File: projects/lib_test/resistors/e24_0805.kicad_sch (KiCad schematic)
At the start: 171 parts

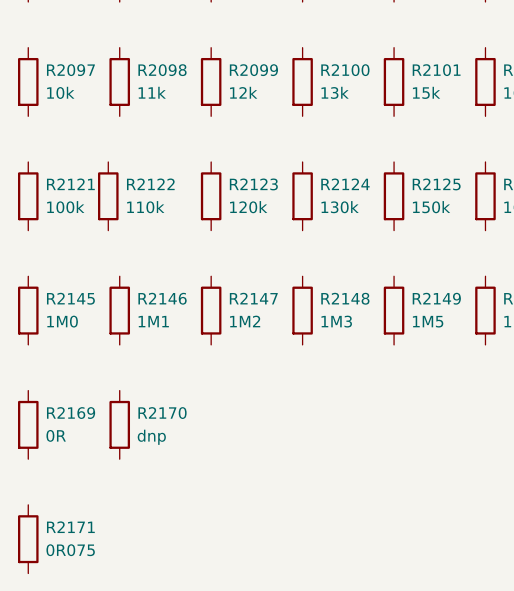
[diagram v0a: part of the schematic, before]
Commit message: add test project for resistors
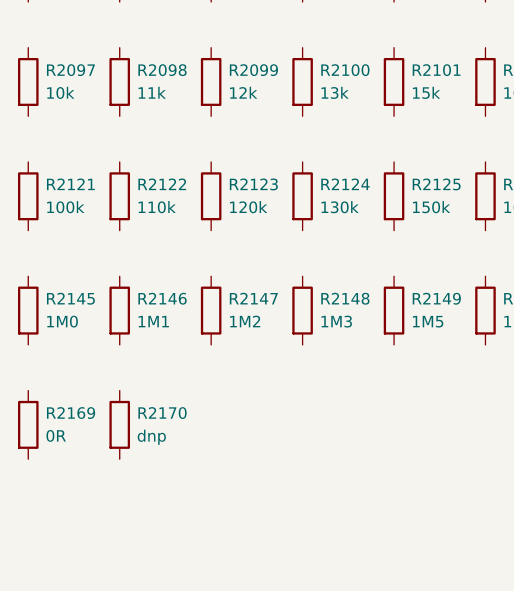
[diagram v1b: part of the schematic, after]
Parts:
- removed R2171: 0R075, lily_footprints:res_2512, symbol lily_symbols:res_0R075_1%_3W_2512
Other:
- company: LilyTronics -> (none)
- title: Lily KiCad Library test -> (none)

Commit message: updated test projects
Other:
- title: (none) -> Resistors
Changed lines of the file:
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@@
 (kicad_sch
-	(version 20231120)
+	(version 20250114)
 	(generator "eeschema")
-	(generator_version "8.0")
+	(generator_version "9.0")
 	(paper "A4")
+	(title_block
+		(title "Resistors")
+		(date "2025-05-24")
+		(rev "1")
+		(comment 1 "-")
+		(comment 2 "-")
+	)
 	(symbol
 		(lib_id "lily_symbols:res_3R3_1%_125mW_0805")

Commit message: updated resistors test design
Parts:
- R2001: JLCPCB_ID C25271 -> C131397; JLCPCB_STATUS Basic -> (none); Lily_ID 1913-11000 -> NO_ID; Manufacturer Uniroyal Electronics -> YAGEO; Manufacturer_ID 0805W8F100KT5E -> RC0805FR-071RL
- R2002: JLCPCB_ID C17376 -> C137574; JLCPCB_STATUS Extended -> (none); Lily_ID 1913-11100 -> NO_ID; Manufacturer Uniroyal Electronics -> YAGEO; Manufacturer_ID 0805W8F110KT5E -> RC0805FR-071R1L
- R2003: JLCPCB_ID C17381 -> C137573; JLCPCB_STATUS Extended -> (none); Lily_ID 1913-11200 -> NO_ID; Manufacturer Uniroyal Electronics -> YAGEO; Manufacturer_ID 0805W8F120KT5E -> RC0805FR-071R2L
- R2004: JLCPCB_ID C17385 -> C185293; JLCPCB_STATUS Extended -> (none); Lily_ID 1913-11300 -> NO_ID; Manufacturer Uniroyal Electronics -> YAGEO; Manufacturer_ID 0805W8F130KT5E -> RC0805FR-071R3L
- R2005: JLCPCB_ID C17392 -> C137572; JLCPCB_STATUS Extended -> (none); Lily_ID 1913-11500 -> NO_ID; Manufacturer Uniroyal Electronics -> YAGEO; Manufacturer_ID 0805W8F150KT5E -> RC0805FR-071R5L
- R2006: JLCPCB_ID C25272 -> C137571; JLCPCB_STATUS Extended -> (none); Lily_ID 1913-11600 -> NO_ID; Manufacturer Uniroyal Electronics -> YAGEO; Manufacturer_ID 0805W8F160KT5E -> RC0805FR-071R6L
- R2007: JLCPCB_ID C17400 -> C327106; JLCPCB_STATUS Extended -> (none); Lily_ID 1913-11800 -> NO_ID; Manufacturer Uniroyal Electronics -> YAGEO; Manufacturer_ID 0805W8F180KT5E -> RC0805FR-071R8L
- R2008: JLCPCB_ID C17606 -> C114246; JLCPCB_STATUS Extended preferred -> (none); Lily_ID 1913-12000 -> NO_ID; Manufacturer Uniroyal Electronics -> YAGEO; Manufacturer_ID 0805W8F200KT5E -> RC0805FR-072RL
- R2009: JLCPCB_ID C17521 -> C137549; JLCPCB_STATUS Basic -> (none); Lily_ID 1913-12200 -> NO_ID; Manufacturer Uniroyal Electronics -> YAGEO; Manufacturer_ID 0805W8F220KT5E -> RC0805FR-072R2L
- R2010: JLCPCB_ID C17528 -> C137548; JLCPCB_STATUS Extended -> (none); Lily_ID 1913-12400 -> NO_ID; Manufacturer Uniroyal Electronics -> YAGEO; Manufacturer_ID 0805W8F240KT5E -> RC0805FR-072R4L
- R2011: JLCPCB_ID C17532 -> C137547; JLCPCB_STATUS Extended -> (none); Lily_ID 1913-12700 -> NO_ID; Manufacturer Uniroyal Electronics -> YAGEO; Manufacturer_ID 0805W8F270KT5E -> RC0805FR-072R7L
- R2012: JLCPCB_ID C17660 -> C137528; JLCPCB_STATUS Extended -> (none); Lily_ID 1913-13000 -> NO_ID; Manufacturer Uniroyal Electronics -> YAGEO; Manufacturer_ID 0805W8F300KT5E -> RC0805FR-073RL
- R2013: JLCPCB_ID C16257 -> C137531; JLCPCB_STATUS Extended -> (none); Lily_ID 1913-13300 -> NO_ID; Manufacturer Uniroyal Electronics -> YAGEO; Manufacturer_ID 0805W8F330KT5E -> RC0805FR-073R3L
- R2014: JLCPCB_ID C17610 -> C137530; JLCPCB_STATUS Extended -> (none); Lily_ID 1913-13600 -> NO_ID; Manufacturer Uniroyal Electronics -> YAGEO; Manufacturer_ID 0805W8F360KT5E -> RC0805FR-073R6L
- R2015: JLCPCB_ID C17615 -> C137529; JLCPCB_STATUS Extended -> (none); Lily_ID 1913-13900 -> NO_ID; Manufacturer Uniroyal Electronics -> YAGEO; Manufacturer_ID 0805W8F390KT5E -> RC0805FR-073R9L
- R2016: JLCPCB_ID C17669 -> C137514; JLCPCB_STATUS Extended -> (none); Lily_ID 1913-14300 -> NO_ID; Manufacturer Uniroyal Electronics -> YAGEO; Manufacturer_ID 0805W8F430KT5E -> RC0805FR-074R3L
- R2017: JLCPCB_ID C17675 -> C137513; JLCPCB_STATUS Basic -> (none); Lily_ID 1913-14700 -> NO_ID; Manufacturer Uniroyal Electronics -> YAGEO; Manufacturer_ID 0805W8F470KT5E -> RC0805FR-074R7L
- R2018: JLCPCB_ID C17724 -> C114539; JLCPCB_STATUS Basic -> (none); Lily_ID 1913-15100 -> NO_ID; Manufacturer Uniroyal Electronics -> YAGEO; Manufacturer_ID 0805W8F510KT5E -> RC0805FR-075R1L
- R2019: JLCPCB_ID C17729 -> C275644; JLCPCB_STATUS Extended -> (none); Lily_ID 1913-15600 -> NO_ID; Manufacturer Uniroyal Electronics -> YAGEO; Manufacturer_ID 0805W8F560KT5E -> RC0805FR-075R6L
- R2020: JLCPCB_ID C17768 -> C483193; JLCPCB_STATUS Extended -> (none); Lily_ID 1913-16200 -> NO_ID; Manufacturer Uniroyal Electronics -> YAGEO; Manufacturer_ID 0805W8F620KT5E -> RC0805FR-076R2L
- R2021: JLCPCB_ID C17774 -> C137492; JLCPCB_STATUS Extended -> (none); Lily_ID 1913-16800 -> NO_ID; Manufacturer Uniroyal Electronics -> YAGEO; Manufacturer_ID 0805W8F680KT5E -> RC0805FR-076R8L
- R2022: JLCPCB_ID C17809 -> C483222; JLCPCB_STATUS Extended -> (none); Lily_ID 1913-17500 -> NO_ID; Manufacturer Uniroyal Electronics -> YAGEO; Manufacturer_ID 0805W8F750KT5E -> RC0805FR-077R5L
- R2023: JLCPCB_ID C17830 -> C185282; JLCPCB_STATUS Extended -> (none); Lily_ID 1913-18200 -> NO_ID; Manufacturer Uniroyal Electronics -> YAGEO; Manufacturer_ID 0805W8F820KT5E -> RC0805FR-078R2L
- R2024: JLCPCB_ID C17857 -> C483254; JLCPCB_STATUS Extended -> (none); Lily_ID 1913-19100 -> NO_ID; Manufacturer Uniroyal Electronics -> YAGEO; Manufacturer_ID 0805W8F910KT5E -> RC0805FR-079R1L
- R2025: JLCPCB_ID C17415 -> C96347; JLCPCB_STATUS Basic -> (none); Lily_ID 1913-11001 -> NO_ID; Manufacturer Uniroyal Electronics -> YAGEO; Manufacturer_ID 0805W8F100JT5E -> RC0805FR-0710RL
- R2026: JLCPCB_ID C17430 -> C185296; JLCPCB_STATUS Extended -> (none); Lily_ID 1913-11101 -> NO_ID; Manufacturer Uniroyal Electronics -> YAGEO; Manufacturer_ID 0805W8F110JT5E -> RC0805FR-0711RL
- R2027: JLCPCB_ID C17445 -> C137594; JLCPCB_STATUS Extended -> (none); Lily_ID 1913-11201 -> NO_ID; Manufacturer Uniroyal Electronics -> YAGEO; Manufacturer_ID 0805W8F120JT5E -> RC0805FR-0712RL
- R2028: JLCPCB_ID C25268 -> C273810; JLCPCB_STATUS Extended -> (none); Lily_ID 1913-11301 -> NO_ID; Manufacturer Uniroyal Electronics -> YAGEO; Manufacturer_ID 0805W8F130JT5E -> RC0805FR-0713RL
- R2029: JLCPCB_ID C17480 -> C137590; JLCPCB_STATUS Extended preferred -> (none); Lily_ID 1913-11501 -> NO_ID; Manufacturer Uniroyal Electronics -> YAGEO; Manufacturer_ID 0805W8F150JT5E -> RC0805FR-0715RL
- R2030: JLCPCB_ID C17491 -> C137587; JLCPCB_STATUS Extended -> (none); Lily_ID 1913-11601 -> NO_ID; Manufacturer Uniroyal Electronics -> YAGEO; Manufacturer_ID 0805W8F160JT5E -> RC0805FR-0716RL
- R2031: JLCPCB_ID C17507 -> C137583; JLCPCB_STATUS Extended -> (none); Lily_ID 1913-11801 -> NO_ID; Manufacturer Uniroyal Electronics -> YAGEO; Manufacturer_ID 0805W8F180JT5E -> RC0805FR-0718RL
- R2032: JLCPCB_ID C17544 -> C114557; JLCPCB_STATUS Basic -> (none); Lily_ID 1913-12001 -> NO_ID; Manufacturer Uniroyal Electronics -> YAGEO; Manufacturer_ID 0805W8F200JT5E -> RC0805FR-0720RL
- R2033: JLCPCB_ID C17561 -> C107702; JLCPCB_STATUS Basic -> (none); Lily_ID 1913-12201 -> NO_ID; Manufacturer Uniroyal Electronics -> YAGEO; Manufacturer_ID 0805W8F220JT5E -> RC0805FR-0722RL
- R2034: JLCPCB_ID C17576 -> C185291; JLCPCB_STATUS Extended -> (none); Lily_ID 1913-12401 -> NO_ID; Manufacturer Uniroyal Electronics -> YAGEO; Manufacturer_ID 0805W8F240JT5E -> RC0805FR-0724RL
- R2035: JLCPCB_ID C17594 -> C163408; JLCPCB_STATUS Extended preferred -> (none); Lily_ID 1913-12701 -> NO_ID; Manufacturer Uniroyal Electronics -> YAGEO; Manufacturer_ID 0805W8F270JT5E -> RC0805FR-0727RL
- R2036: JLCPCB_ID C17622 -> C137545; JLCPCB_STATUS Extended -> (none); Lily_ID 1913-13001 -> NO_ID; Manufacturer Uniroyal Electronics -> YAGEO; Manufacturer_ID 0805W8F300JT5E -> RC0805FR-0730RL
- R2037: JLCPCB_ID C17634 -> C126353; JLCPCB_STATUS Basic -> (none); Lily_ID 1913-13301 -> NO_ID; Manufacturer Uniroyal Electronics -> YAGEO; Manufacturer_ID 0805W8F330JT5E -> RC0805FR-0733RL
- R2038: JLCPCB_ID C36524 -> C137536; JLCPCB_STATUS Extended -> (none); Lily_ID 1913-13601 -> NO_ID; Manufacturer Uniroyal Electronics -> YAGEO; Manufacturer_ID 0805W8F360JT5E -> RC0805FR-0736RL
- R2039: JLCPCB_ID C17659 -> C137534; JLCPCB_STATUS Extended -> (none); Lily_ID 1913-13901 -> NO_ID; Manufacturer Uniroyal Electronics -> YAGEO; Manufacturer_ID 0805W8F390JT5E -> RC0805FR-0739RL
- R2040: JLCPCB_ID C4368 -> C137523; JLCPCB_STATUS Extended -> (none); Lily_ID 1913-14301 -> NO_ID; Manufacturer Uniroyal Electronics -> YAGEO; Manufacturer_ID 0805W8F430JT5E -> RC0805FR-0743RL
- R2041: JLCPCB_ID C17714 -> C114541; JLCPCB_STATUS Basic -> (none); Lily_ID 1913-14701 -> NO_ID; Manufacturer Uniroyal Electronics -> YAGEO; Manufacturer_ID 0805W8F470JT5E -> RC0805FR-0747RL
- R2042: JLCPCB_ID C17738 -> C114537; JLCPCB_STATUS Basic -> (none); Lily_ID 1913-15101 -> NO_ID; Manufacturer Uniroyal Electronics -> YAGEO; Manufacturer_ID 0805W8F510JT5E -> RC0805FR-0751RL
- R2043: JLCPCB_ID C17757 -> C137507; JLCPCB_STATUS Extended preferred -> (none); Lily_ID 1913-15601 -> NO_ID; Manufacturer Uniroyal Electronics -> YAGEO; Manufacturer_ID 0805W8F560JT5E -> RC0805FR-0756RL
- R2044: JLCPCB_ID C17784 -> C185283; JLCPCB_STATUS Extended -> (none); Lily_ID 1913-16201 -> NO_ID; Manufacturer Uniroyal Electronics -> YAGEO; Manufacturer_ID 0805W8F620JT5E -> RC0805FR-0762RL
- R2045: JLCPCB_ID C17802 -> C137498; JLCPCB_STATUS Extended preferred -> (none); Lily_ID 1913-16801 -> NO_ID; Manufacturer Uniroyal Electronics -> YAGEO; Manufacturer_ID 0805W8F680JT5E -> RC0805FR-0768RL
- R2046: JLCPCB_ID C17820 -> C141697; JLCPCB_STATUS Extended -> (none); Lily_ID 1913-17501 -> NO_ID; Manufacturer Uniroyal Electronics -> YAGEO; Manufacturer_ID 0805W8F750JT5E -> RC0805FR-0775RL
- R2047: JLCPCB_ID C17841 -> C141699; JLCPCB_STATUS Extended -> (none); Lily_ID 1913-18201 -> NO_ID; Manufacturer Uniroyal Electronics -> YAGEO; Manufacturer_ID 0805W8F820JT5E -> RC0805FR-0782RL
- R2048: JLCPCB_ID C4407 -> C276315; JLCPCB_STATUS Extended -> (none); Lily_ID 1913-19101 -> NO_ID; Manufacturer Uniroyal Electronics -> YAGEO; Manufacturer_ID 0805W8F910JT5E -> RC0805FR-0791RL
- R2049: JLCPCB_ID C17408 -> C105577; JLCPCB_STATUS Basic -> (none); Lily_ID 1913-11002 -> NO_ID; Manufacturer Uniroyal Electronics -> YAGEO; Manufacturer_ID 0805W8F1000T5E -> RC0805FR-07100RL
- R2050: JLCPCB_ID C17423 -> C246031; JLCPCB_STATUS Extended -> (none); Lily_ID 1913-11102 -> NO_ID; Manufacturer Uniroyal Electronics -> YAGEO; Manufacturer_ID 0805W8F1100T5E -> RC0805FR-07110RL
- R2051: JLCPCB_ID C17437 -> C114245; JLCPCB_STATUS Basic -> (none); Lily_ID 1913-11202 -> NO_ID; Manufacturer Uniroyal Electronics -> YAGEO; Manufacturer_ID 0805W8F1200T5E -> RC0805FR-07120RL
- R2052: JLCPCB_ID C17451 -> C273821; JLCPCB_STATUS Extended -> (none); Lily_ID 1913-11302 -> NO_ID; Manufacturer Uniroyal Electronics -> YAGEO; Manufacturer_ID 0805W8F1300T5E -> RC0805FR-07130RL
- R2053: JLCPCB_ID C17471 -> C114523; JLCPCB_STATUS Basic -> (none); Lily_ID 1913-11502 -> NO_ID; Manufacturer Uniroyal Electronics -> YAGEO; Manufacturer_ID 0805W8F1500T5E -> RC0805FR-07150RL
- R2054: JLCPCB_ID C25269 -> C246032; JLCPCB_STATUS Extended -> (none); Lily_ID 1913-11602 -> NO_ID; Manufacturer Uniroyal Electronics -> YAGEO; Manufacturer_ID 0805W8F1600T5E -> RC0805FR-07160RL
- R2055: JLCPCB_ID C25270 -> C137585; JLCPCB_STATUS Extended preferred -> (none); Lily_ID 1913-11802 -> NO_ID; Manufacturer Uniroyal Electronics -> YAGEO; Manufacturer_ID 0805W8F1800T5E -> RC0805FR-07180RL
- R2056: JLCPCB_ID C17540 -> C114567; JLCPCB_STATUS Basic -> (none); Lily_ID 1913-12002 -> NO_ID; Manufacturer Uniroyal Electronics -> YAGEO; Manufacturer_ID 0805W8F2000T5E -> RC0805FR-07200RL
- R2057: JLCPCB_ID C17557 -> C114519; JLCPCB_STATUS Basic -> (none); Lily_ID 1913-12202 -> NO_ID; Manufacturer Uniroyal Electronics -> YAGEO; Manufacturer_ID 0805W8F2200T5E -> RC0805FR-07220RL
- R2058: JLCPCB_ID C17572 -> C185292; JLCPCB_STATUS Extended preferred -> (none); Lily_ID 1913-12402 -> NO_ID; Manufacturer Uniroyal Electronics -> YAGEO; Manufacturer_ID 0805W8F2400T5E -> RC0805FR-07240RL
- R2059: JLCPCB_ID C17590 -> C137558; JLCPCB_STATUS Extended preferred -> (none); Lily_ID 1913-12702 -> NO_ID; Manufacturer Uniroyal Electronics -> YAGEO; Manufacturer_ID 0805W8F2700T5E -> RC0805FR-07270RL
- R2060: JLCPCB_ID C17617 -> C114529; JLCPCB_STATUS Basic -> (none); Lily_ID 1913-13002 -> NO_ID; Manufacturer Uniroyal Electronics -> YAGEO; Manufacturer_ID 0805W8F3000T5E -> RC0805FR-07300RL
- R2061: JLCPCB_ID C17630 -> C105878; JLCPCB_STATUS Basic -> (none); Lily_ID 1913-13302 -> NO_ID; Manufacturer Uniroyal Electronics -> YAGEO; Manufacturer_ID 0805W8F3300T5E -> RC0805FR-07330RL
- R2062: JLCPCB_ID C17646 -> C137538; JLCPCB_STATUS Extended -> (none); Lily_ID 1913-13602 -> NO_ID; Manufacturer Uniroyal Electronics -> YAGEO; Manufacturer_ID 0805W8F3600T5E -> RC0805FR-07360RL
- R2063: JLCPCB_ID C17655 -> C114543; JLCPCB_STATUS Basic -> (none); Lily_ID 1913-13902 -> NO_ID; Manufacturer Uniroyal Electronics -> YAGEO; Manufacturer_ID 0805W8F3900T5E -> RC0805FR-07390RL
- R2064: JLCPCB_ID C42000 -> C137527; JLCPCB_STATUS Extended -> (none); Lily_ID 1913-14302 -> NO_ID; Manufacturer Uniroyal Electronics -> YAGEO; Manufacturer_ID 0805W8F4300T5E -> RC0805FR-07430RL
- R2065: JLCPCB_ID C17710 -> C114564; JLCPCB_STATUS Basic -> (none); Lily_ID 1913-14702 -> NO_ID; Manufacturer Uniroyal Electronics -> YAGEO; Manufacturer_ID 0805W8F4700T5E -> RC0805FR-07470RL
- R2066: JLCPCB_ID C17734 -> C114563; JLCPCB_STATUS Basic -> (none); Lily_ID 1913-15102 -> NO_ID; Manufacturer Uniroyal Electronics -> YAGEO; Manufacturer_ID 0805W8F5100T5E -> RC0805FR-07510RL
- R2067: JLCPCB_ID C28636 -> C114536; JLCPCB_STATUS Basic -> (none); Lily_ID 1913-15602 -> NO_ID; Manufacturer Uniroyal Electronics -> YAGEO; Manufacturer_ID 0805W8F5600T5E -> RC0805FR-07560RL
- R2068: JLCPCB_ID C17782 -> C137503; JLCPCB_STATUS Extended -> (none); Lily_ID 1913-16202 -> NO_ID; Manufacturer Uniroyal Electronics -> YAGEO; Manufacturer_ID 0805W8F6200T5E -> RC0805FR-07620RL
- R2069: JLCPCB_ID C17798 -> C114549; JLCPCB_STATUS Basic -> (none); Lily_ID 1913-16802 -> NO_ID; Manufacturer Uniroyal Electronics -> YAGEO; Manufacturer_ID 0805W8F6800T5E -> RC0805FR-07680RL
- R2070: JLCPCB_ID C17818 -> C114546; JLCPCB_STATUS Extended preferred -> (none); Lily_ID 1913-17502 -> NO_ID; Manufacturer Uniroyal Electronics -> YAGEO; Manufacturer_ID 0805W8F7500T5E -> RC0805FR-07750RL
- R2071: JLCPCB_ID C17837 -> C114544; JLCPCB_STATUS Extended preferred -> (none); Lily_ID 1913-18202 -> NO_ID; Manufacturer Uniroyal Electronics -> YAGEO; Manufacturer_ID 0805W8F8200T5E -> RC0805FR-07820RL
- R2072: JLCPCB_ID C17865 -> C141702; JLCPCB_STATUS Extended -> (none); Lily_ID 1913-19102 -> NO_ID; Manufacturer Uniroyal Electronics -> YAGEO; Manufacturer_ID 0805W8F9100T5E -> RC0805FR-07910RL
- R2073: JLCPCB_ID C17513 -> C95781; JLCPCB_STATUS Basic -> (none); Lily_ID 1913-11003 -> NO_ID; Manufacturer Uniroyal Electronics -> YAGEO; Manufacturer_ID 0805W8F1001T5E -> RC0805FR-071KL
- R2074: JLCPCB_ID C17375 -> C185294; JLCPCB_STATUS Extended -> (none); Lily_ID 1913-11103 -> NO_ID; Manufacturer Uniroyal Electronics -> YAGEO; Manufacturer_ID 0805W8F1101T5E -> RC0805FR-071K1L
- R2075: JLCPCB_ID C17379 -> C114526; JLCPCB_STATUS Basic -> (none); Lily_ID 1913-11203 -> NO_ID; Manufacturer Uniroyal Electronics -> YAGEO; Manufacturer_ID 0805W8F1201T5E -> RC0805FR-071K2L
- R2076: JLCPCB_ID C17384 -> C137582; JLCPCB_STATUS Extended -> (none); Lily_ID 1913-11303 -> NO_ID; Manufacturer Uniroyal Electronics -> YAGEO; Manufacturer_ID 0805W8F1301T5E -> RC0805FR-071K3L
- R2077: JLCPCB_ID C4310 -> C114555; JLCPCB_STATUS Basic -> (none); Lily_ID 1913-11503 -> NO_ID; Manufacturer Uniroyal Electronics -> YAGEO; Manufacturer_ID 0805W8F1501T5E -> RC0805FR-071K5L
- R2078: JLCPCB_ID C17394 -> C137580; JLCPCB_STATUS Extended -> (none); Lily_ID 1913-11603 -> NO_ID; Manufacturer Uniroyal Electronics -> YAGEO; Manufacturer_ID 0805W8F1601T5E -> RC0805FR-071K6L
- R2079: JLCPCB_ID C17398 -> C137579; JLCPCB_STATUS Extended preferred -> (none); Lily_ID 1913-11803 -> NO_ID; Manufacturer Uniroyal Electronics -> YAGEO; Manufacturer_ID 0805W8F1801T5E -> RC0805FR-071K8L
- R2080: JLCPCB_ID C17604 -> C114572; JLCPCB_STATUS Basic -> (none); Lily_ID 1913-12003 -> NO_ID; Manufacturer Uniroyal Electronics -> YAGEO; Manufacturer_ID 0805W8F2001T5E -> RC0805FR-072KL
- R2081: JLCPCB_ID C17520 -> C114561; JLCPCB_STATUS Basic -> (none); Lily_ID 1913-12203 -> NO_ID; Manufacturer Uniroyal Electronics -> YAGEO; Manufacturer_ID 0805W8F2201T5E -> RC0805FR-072K2L
- R2082: JLCPCB_ID C17526 -> C114521; JLCPCB_STATUS Basic -> (none); Lily_ID 1913-12403 -> NO_ID; Manufacturer Uniroyal Electronics -> YAGEO; Manufacturer_ID 0805W8F2401T5E -> RC0805FR-072K4L
- R2083: JLCPCB_ID C17530 -> C114520; JLCPCB_STATUS Basic -> (none); Lily_ID 1913-12703 -> NO_ID; Manufacturer Uniroyal Electronics -> YAGEO; Manufacturer_ID 0805W8F2701T5E -> RC0805FR-072K7L
- R2084: JLCPCB_ID C17661 -> C126350; JLCPCB_STATUS Basic -> (none); Lily_ID 1913-13003 -> NO_ID; Manufacturer Uniroyal Electronics -> YAGEO; Manufacturer_ID 0805W8F3001T5E -> RC0805FR-073KL
- R2085: JLCPCB_ID C26010 -> C114531; JLCPCB_STATUS Basic -> (none); Lily_ID 1913-13303 -> NO_ID; Manufacturer Uniroyal Electronics -> YAGEO; Manufacturer_ID 0805W8F3301T5E -> RC0805FR-073K3L
- R2086: JLCPCB_ID C18359 -> C137533; JLCPCB_STATUS Extended preferred -> (none); Lily_ID 1913-13603 -> NO_ID; Manufacturer Uniroyal Electronics -> YAGEO; Manufacturer_ID 0805W8F3601T5E -> RC0805FR-073K6L
- R2087: JLCPCB_ID C17614 -> C114221; JLCPCB_STATUS Basic -> (none); Lily_ID 1913-13903 -> NO_ID; Manufacturer Uniroyal Electronics -> YAGEO; Manufacturer_ID 0805W8F3901T5E -> RC0805FR-073K9L
- R2088: JLCPCB_ID C17667 -> C137518; JLCPCB_STATUS Extended preferred -> (none); Lily_ID 1913-14303 -> NO_ID; Manufacturer Uniroyal Electronics -> YAGEO; Manufacturer_ID 0805W8F4301T5E -> RC0805FR-074K3L
- R2089: JLCPCB_ID C17673 -> C60816; JLCPCB_STATUS Basic -> (none); Lily_ID 1913-14703 -> NO_ID; Manufacturer Uniroyal Electronics -> YAGEO; Manufacturer_ID 0805W8F4701T5E -> RC0805FR-074K7L
- R2090: JLCPCB_ID C27834 -> C84375; JLCPCB_STATUS Basic -> (none); Lily_ID 1913-15103 -> NO_ID; Manufacturer Uniroyal Electronics -> YAGEO; Manufacturer_ID 0805W8F5101T5E -> RC0805FR-075K1L
- R2091: JLCPCB_ID C4382 -> C114538; JLCPCB_STATUS Basic -> (none); Lily_ID 1913-15603 -> NO_ID; Manufacturer Uniroyal Electronics -> YAGEO; Manufacturer_ID 0805W8F5601T5E -> RC0805FR-075K6L
- R2092: JLCPCB_ID C17767 -> C114535; JLCPCB_STATUS Extended preferred -> (none); Lily_ID 1913-16203 -> NO_ID; Manufacturer Uniroyal Electronics -> YAGEO; Manufacturer_ID 0805W8F6201T5E -> RC0805FR-076K2L
- R2093: JLCPCB_ID C17772 -> C114550; JLCPCB_STATUS Basic -> (none); Lily_ID 1913-16803 -> NO_ID; Manufacturer Uniroyal Electronics -> YAGEO; Manufacturer_ID 0805W8F6801T5E -> RC0805FR-076K8L
- R2094: JLCPCB_ID C17807 -> C114547; JLCPCB_STATUS Extended preferred -> (none); Lily_ID 1913-17503 -> NO_ID; Manufacturer Uniroyal Electronics -> YAGEO; Manufacturer_ID 0805W8F7501T5E -> RC0805FR-077K5L
- R2095: JLCPCB_ID C17828 -> C114545; JLCPCB_STATUS Basic -> (none); Lily_ID 1913-18203 -> NO_ID; Manufacturer Uniroyal Electronics -> YAGEO; Manufacturer_ID 0805W8F8201T5E -> RC0805FR-078K2L
- R2096: JLCPCB_ID C17855 -> C137482; JLCPCB_STATUS Extended preferred -> (none); Lily_ID 1913-19103 -> NO_ID; Manufacturer Uniroyal Electronics -> YAGEO; Manufacturer_ID 0805W8F9101T5E -> RC0805FR-079K1L
- R2097: JLCPCB_ID C17414 -> C84376; JLCPCB_STATUS Basic -> (none); Lily_ID 1913-11004 -> NO_ID; Manufacturer Uniroyal Electronics -> YAGEO; Manufacturer_ID 0805W8F1002T5E -> RC0805FR-0710KL
- R2098: JLCPCB_ID C17429 -> C137597; JLCPCB_STATUS Extended preferred -> (none); Lily_ID 1913-11104 -> NO_ID; Manufacturer Uniroyal Electronics -> YAGEO; Manufacturer_ID 0805W8F1102T5E -> RC0805FR-0711KL
- R2099: JLCPCB_ID C17444 -> C114556; JLCPCB_STATUS Basic -> (none); Lily_ID 1913-11204 -> NO_ID; Manufacturer Uniroyal Electronics -> YAGEO; Manufacturer_ID 0805W8F1202T5E -> RC0805FR-0712KL
- R2100: JLCPCB_ID C17455 -> C137592; JLCPCB_STATUS Extended preferred -> (none); Lily_ID 1913-11304 -> NO_ID; Manufacturer Uniroyal Electronics -> YAGEO; Manufacturer_ID 0805W8F1302T5E -> RC0805FR-0713KL
- R2101: JLCPCB_ID C17475 -> C114559; JLCPCB_STATUS Basic -> (none); Lily_ID 1913-11504 -> NO_ID; Manufacturer Uniroyal Electronics -> YAGEO; Manufacturer_ID 0805W8F1502T5E -> RC0805FR-0715KL
- R2102: JLCPCB_ID C17490 -> C137588; JLCPCB_STATUS Extended preferred -> (none); Lily_ID 1913-11604 -> NO_ID; Manufacturer Uniroyal Electronics -> YAGEO; Manufacturer_ID 0805W8F1602T5E -> RC0805FR-0716KL
- R2103: JLCPCB_ID C17506 -> C114522; JLCPCB_STATUS Extended preferred -> (none); Lily_ID 1913-11804 -> NO_ID; Manufacturer Uniroyal Electronics -> YAGEO; Manufacturer_ID 0805W8F1802T5E -> RC0805FR-0718KL
- R2104: JLCPCB_ID C4328 -> C114566; JLCPCB_STATUS Basic -> (none); Lily_ID 1913-12004 -> NO_ID; Manufacturer Uniroyal Electronics -> YAGEO; Manufacturer_ID 0805W8F2002T5E -> RC0805FR-0720KL
- R2105: JLCPCB_ID C17560 -> C114565; JLCPCB_STATUS Basic -> (none); Lily_ID 1913-12204 -> NO_ID; Manufacturer Uniroyal Electronics -> YAGEO; Manufacturer_ID 0805W8F2202T5E -> RC0805FR-0722KL
- R2106: JLCPCB_ID C17575 -> C137562; JLCPCB_STATUS Basic -> (none); Lily_ID 1913-12404 -> NO_ID; Manufacturer Uniroyal Electronics -> YAGEO; Manufacturer_ID 0805W8F2402T5E -> RC0805FR-0724KL
- R2107: JLCPCB_ID C17593 -> C114533; JLCPCB_STATUS Basic -> (none); Lily_ID 1913-12704 -> NO_ID; Manufacturer Uniroyal Electronics -> YAGEO; Manufacturer_ID 0805W8F2702T5E -> RC0805FR-0727KL
- R2108: JLCPCB_ID C17621 -> C126352; JLCPCB_STATUS Basic -> (none); Lily_ID 1913-13004 -> NO_ID; Manufacturer Uniroyal Electronics -> YAGEO; Manufacturer_ID 0805W8F3002T5E -> RC0805FR-0730KL
- R2109: JLCPCB_ID C17633 -> C141696; JLCPCB_STATUS Basic -> (none); Lily_ID 1913-13304 -> NO_ID; Manufacturer Uniroyal Electronics -> YAGEO; Manufacturer_ID 0805W8F3302T5E -> RC0805FR-0733KL
- R2110: JLCPCB_ID C4360 -> C114527; JLCPCB_STATUS Extended preferred -> (none); Lily_ID 1913-13604 -> NO_ID; Manufacturer Uniroyal Electronics -> YAGEO; Manufacturer_ID 0805W8F3602T5E -> RC0805FR-0736KL
- R2111: JLCPCB_ID C25826 -> C113306; JLCPCB_STATUS Extended preferred -> (none); Lily_ID 1913-13904 -> NO_ID; Manufacturer Uniroyal Electronics -> YAGEO; Manufacturer_ID 0805W8F3902T5E -> RC0805FR-0739KL
- R2112: JLCPCB_ID C17695 -> C137524; JLCPCB_STATUS Extended preferred -> (none); Lily_ID 1913-14304 -> NO_ID; Manufacturer Uniroyal Electronics -> YAGEO; Manufacturer_ID 0805W8F4302T5E -> RC0805FR-0743KL
- R2113: JLCPCB_ID C17713 -> C126351; JLCPCB_STATUS Basic -> (none); Lily_ID 1913-14704 -> NO_ID; Manufacturer Uniroyal Electronics -> YAGEO; Manufacturer_ID 0805W8F4702T5E -> RC0805FR-0747KL
- R2114: JLCPCB_ID C17737 -> C107233; JLCPCB_STATUS Basic -> (none); Lily_ID 1913-15104 -> NO_ID; Manufacturer Uniroyal Electronics -> YAGEO; Manufacturer_ID 0805W8F5102T5E -> RC0805FR-0751KL
- R2115: JLCPCB_ID C17756 -> C137509; JLCPCB_STATUS Extended preferred -> (none); Lily_ID 1913-15604 -> NO_ID; Manufacturer Uniroyal Electronics -> YAGEO; Manufacturer_ID 0805W8F5602T5E -> RC0805FR-0756KL
- R2116: JLCPCB_ID C17783 -> C137502; JLCPCB_STATUS Extended preferred -> (none); Lily_ID 1913-16204 -> NO_ID; Manufacturer Uniroyal Electronics -> YAGEO; Manufacturer_ID 0805W8F6202T5E -> RC0805FR-0762KL
- R2117: JLCPCB_ID C17801 -> C114548; JLCPCB_STATUS Basic -> (none); Lily_ID 1913-16804 -> NO_ID; Manufacturer Uniroyal Electronics -> YAGEO; Manufacturer_ID 0805W8F6802T5E -> RC0805FR-0768KL
- R2118: JLCPCB_ID C17819 -> C137491; JLCPCB_STATUS Extended preferred -> (none); Lily_ID 1913-17504 -> NO_ID; Manufacturer Uniroyal Electronics -> YAGEO; Manufacturer_ID 0805W8F7502T5E -> RC0805FR-0775KL
- R2119: JLCPCB_ID C17840 -> C137489; JLCPCB_STATUS Extended preferred -> (none); Lily_ID 1913-18204 -> NO_ID; Manufacturer Uniroyal Electronics -> YAGEO; Manufacturer_ID 0805W8F8202T5E -> RC0805FR-0782KL
- R2120: JLCPCB_ID C17866 -> C137484; JLCPCB_STATUS Extended -> (none); Lily_ID 1913-19104 -> NO_ID; Manufacturer Uniroyal Electronics -> YAGEO; Manufacturer_ID 0805W8F9102T5E -> RC0805FR-0791KL
- R2121: JLCPCB_ID C149504 -> C96346; JLCPCB_STATUS Basic -> (none); Lily_ID 1913-11005 -> NO_ID; Manufacturer Uniroyal Electronics -> YAGEO; Manufacturer_ID 0805W8F1003T5E -> RC0805FR-07100KL
- R2122: JLCPCB_ID C17422 -> C137599; JLCPCB_STATUS Extended -> (none); Lily_ID 1913-11105 -> NO_ID; Manufacturer Uniroyal Electronics -> YAGEO; Manufacturer_ID 0805W8F1103T5E -> RC0805FR-07110KL
- R2123: JLCPCB_ID C17436 -> C114524; JLCPCB_STATUS Extended preferred -> (none); Lily_ID 1913-11205 -> NO_ID; Manufacturer Uniroyal Electronics -> YAGEO; Manufacturer_ID 0805W8F1203T5E -> RC0805FR-07120KL
- R2124: JLCPCB_ID C17450 -> C483008; JLCPCB_STATUS Extended -> (none); Lily_ID 1913-11305 -> NO_ID; Manufacturer Uniroyal Electronics -> YAGEO; Manufacturer_ID 0805W8F1303T5E -> RC0805FR-07130KL
- R2125: JLCPCB_ID C17470 -> C114558; JLCPCB_STATUS Basic -> (none); Lily_ID 1913-11505 -> NO_ID; Manufacturer Uniroyal Electronics -> YAGEO; Manufacturer_ID 0805W8F1503T5E -> RC0805FR-07150KL
- R2126: JLCPCB_ID C17485 -> C185295; JLCPCB_STATUS Extended -> (none); Lily_ID 1913-11605 -> NO_ID; Manufacturer Uniroyal Electronics -> YAGEO; Manufacturer_ID 0805W8F1603T5E -> RC0805FR-07160KL
- R2127: JLCPCB_ID C17501 -> C137586; JLCPCB_STATUS Extended preferred -> (none); Lily_ID 1913-11805 -> NO_ID; Manufacturer Uniroyal Electronics -> YAGEO; Manufacturer_ID 0805W8F1803T5E -> RC0805FR-07180KL
- R2128: JLCPCB_ID C17539 -> C114562; JLCPCB_STATUS Basic -> (none); Lily_ID 1913-12005 -> NO_ID; Manufacturer Uniroyal Electronics -> YAGEO; Manufacturer_ID 0805W8F2003T5E -> RC0805FR-07200KL
- R2129: JLCPCB_ID C17556 -> C137568; JLCPCB_STATUS Basic -> (none); Lily_ID 1913-12205 -> NO_ID; Manufacturer Uniroyal Electronics -> YAGEO; Manufacturer_ID 0805W8F2203T5E -> RC0805FR-07220KL
- R2130: JLCPCB_ID C25824 -> C137564; JLCPCB_STATUS Extended -> (none); Lily_ID 1913-12405 -> NO_ID; Manufacturer Uniroyal Electronics -> YAGEO; Manufacturer_ID 0805W8F2403T5E -> RC0805FR-07240KL
- R2131: JLCPCB_ID C17589 -> C137559; JLCPCB_STATUS Extended preferred -> (none); Lily_ID 1913-12705 -> NO_ID; Manufacturer Uniroyal Electronics -> YAGEO; Manufacturer_ID 0805W8F2703T5E -> RC0805FR-07270KL
- R2132: JLCPCB_ID C17616 -> C114530; JLCPCB_STATUS Extended preferred -> (none); Lily_ID 1913-13005 -> NO_ID; Manufacturer Uniroyal Electronics -> YAGEO; Manufacturer_ID 0805W8F3003T5E -> RC0805FR-07300KL
- R2133: JLCPCB_ID C17629 -> C114528; JLCPCB_STATUS Extended preferred -> (none); Lily_ID 1913-13305 -> NO_ID; Manufacturer Uniroyal Electronics -> YAGEO; Manufacturer_ID 0805W8F3303T5E -> RC0805FR-07330KL
- R2134: JLCPCB_ID C17645 -> C137539; JLCPCB_STATUS Extended -> (none); Lily_ID 1913-13605 -> NO_ID; Manufacturer Uniroyal Electronics -> YAGEO; Manufacturer_ID 0805W8F3603T5E -> RC0805FR-07360KL
- R2135: JLCPCB_ID C17656 -> C137535; JLCPCB_STATUS Extended preferred -> (none); Lily_ID 1913-13905 -> NO_ID; Manufacturer Uniroyal Electronics -> YAGEO; Manufacturer_ID 0805W8F3903T5E -> RC0805FR-07390KL
- R2136: JLCPCB_ID C17692 -> C185287; JLCPCB_STATUS Extended -> (none); Lily_ID 1913-14305 -> NO_ID; Manufacturer Uniroyal Electronics -> YAGEO; Manufacturer_ID 0805W8F4303T5E -> RC0805FR-07430KL
- R2137: JLCPCB_ID C17709 -> C89104; JLCPCB_STATUS Basic -> (none); Lily_ID 1913-14705 -> NO_ID; Manufacturer Uniroyal Electronics -> YAGEO; Manufacturer_ID 0805W8F4703T5E -> RC0805FR-07470KL
- R2138: JLCPCB_ID C17733 -> C137512; JLCPCB_STATUS Extended preferred -> (none); Lily_ID 1913-15105 -> NO_ID; Manufacturer Uniroyal Electronics -> YAGEO; Manufacturer_ID 0805W8F5103T5E -> RC0805FR-07510KL
- R2139: JLCPCB_ID C15785 -> C185286; JLCPCB_STATUS Extended -> (none); Lily_ID 1913-15605 -> NO_ID; Manufacturer Uniroyal Electronics -> YAGEO; Manufacturer_ID 0805W8F5603T5E -> RC0805FR-07560KL
- R2140: JLCPCB_ID C25827 -> C185284; JLCPCB_STATUS Extended -> (none); Lily_ID 1913-16205 -> NO_ID; Manufacturer Uniroyal Electronics -> YAGEO; Manufacturer_ID 0805W8F6203T5E -> RC0805FR-07620KL
- R2141: JLCPCB_ID C17797 -> C137499; JLCPCB_STATUS Extended preferred -> (none); Lily_ID 1913-16805 -> NO_ID; Manufacturer Uniroyal Electronics -> YAGEO; Manufacturer_ID 0805W8F6803T5E -> RC0805FR-07680KL
- R2142: JLCPCB_ID C17817 -> C141698; JLCPCB_STATUS Extended -> (none); Lily_ID 1913-17505 -> NO_ID; Manufacturer Uniroyal Electronics -> YAGEO; Manufacturer_ID 0805W8F7503T5E -> RC0805FR-07750KL
- R2143: JLCPCB_ID C50136 -> C141700; JLCPCB_STATUS Extended -> (none); Lily_ID 1913-18205 -> NO_ID; Manufacturer Uniroyal Electronics -> YAGEO; Manufacturer_ID 0805W8F8203T5E -> RC0805FR-07820KL
- R2144: JLCPCB_ID C17864 -> C141703; JLCPCB_STATUS Extended -> (none); Lily_ID 1913-19105 -> NO_ID; Manufacturer Uniroyal Electronics -> YAGEO; Manufacturer_ID 0805W8F9103T5E -> RC0805FR-07910KL
- R2145: JLCPCB_ID C17514 -> C107700; JLCPCB_STATUS Basic -> (none); Lily_ID 1913-11006 -> NO_ID; Manufacturer Uniroyal Electronics -> YAGEO; Manufacturer_ID 0805W8F1004T5E -> RC0805FR-071ML
- R2146: JLCPCB_ID C62137 -> C137577; JLCPCB_STATUS Extended -> (none); Lily_ID 1913-11106 -> NO_ID; Manufacturer Uniroyal Electronics -> YAGEO; Manufacturer_ID 0805W8F1104T5E -> RC0805FR-071M1L
- R2147: JLCPCB_ID C17380 -> C470025; JLCPCB_STATUS Extended -> (none); Lily_ID 1913-11206 -> NO_ID; Manufacturer Uniroyal Electronics -> YAGEO; Manufacturer_ID 0805W8F1204T5E -> RC0805FR-071M2L
- R2148: JLCPCB_ID C26109 -> C482961; JLCPCB_STATUS Extended -> (none); Lily_ID 1913-11306 -> NO_ID; Manufacturer Uniroyal Electronics -> YAGEO; Manufacturer_ID 0805W8F1304T5E -> RC0805FR-071M3L
- R2149: JLCPCB_ID C26110 -> C275642; JLCPCB_STATUS Extended -> (none); Lily_ID 1913-11506 -> NO_ID; Manufacturer Uniroyal Electronics -> YAGEO; Manufacturer_ID 0805W8F1504T5E -> RC0805FR-071M5L
- R2150: JLCPCB_ID C26111 -> C482979; JLCPCB_STATUS Extended -> (none); Lily_ID 1913-11606 -> NO_ID; Manufacturer Uniroyal Electronics -> YAGEO; Manufacturer_ID 0805W8F1604T5E -> RC0805FR-071M6L
- R2151: JLCPCB_ID C17399 -> C137575; JLCPCB_STATUS Extended -> (none); Lily_ID 1913-11806 -> NO_ID; Manufacturer Uniroyal Electronics -> YAGEO; Manufacturer_ID 0805W8F1804T5E -> RC0805FR-071M8L
- R2152: JLCPCB_ID C26112 -> C114532; JLCPCB_STATUS Extended preferred -> (none); Lily_ID 1913-12006 -> NO_ID; Manufacturer Uniroyal Electronics -> YAGEO; Manufacturer_ID 0805W8F2004T5E -> RC0805FR-072ML
- R2153: JLCPCB_ID C26113 -> C137552; JLCPCB_STATUS Extended preferred -> (none); Lily_ID 1913-12206 -> NO_ID; Manufacturer Uniroyal Electronics -> YAGEO; Manufacturer_ID 0805W8F2204T5E -> RC0805FR-072M2L
- R2154: JLCPCB_ID C17527 -> C137551; JLCPCB_STATUS Extended -> (none); Lily_ID 1913-12406 -> NO_ID; Manufacturer Uniroyal Electronics -> YAGEO; Manufacturer_ID 0805W8F2404T5E -> RC0805FR-072M4L
- R2155: JLCPCB_ID C17531 -> C483057; JLCPCB_STATUS Extended -> (none); Lily_ID 1913-12706 -> NO_ID; Manufacturer Uniroyal Electronics -> YAGEO; Manufacturer_ID 0805W8F2704T5E -> RC0805FR-072M7L
- R2156: JLCPCB_ID C17662 -> C483132; JLCPCB_STATUS Extended -> (none); Lily_ID 1913-13006 -> NO_ID; Manufacturer Uniroyal Electronics -> YAGEO; Manufacturer_ID 0805W8F3004T5E -> RC0805FR-073ML
- R2157: JLCPCB_ID C34154 -> C246033; JLCPCB_STATUS Extended -> (none); Lily_ID 1913-13306 -> NO_ID; Manufacturer Uniroyal Electronics -> YAGEO; Manufacturer_ID 0805W8F3304T5E -> RC0805FR-073M3L
- R2158: JLCPCB_ID C35710 -> C185289; JLCPCB_STATUS Extended -> (none); Lily_ID 1913-13606 -> NO_ID; Manufacturer Uniroyal Electronics -> YAGEO; Manufacturer_ID 0805W8F3604T5E -> RC0805FR-073M6L
- R2159: JLCPCB_ID C35709 -> C185288; JLCPCB_STATUS Extended -> (none); Lily_ID 1913-13906 -> NO_ID; Manufacturer Uniroyal Electronics -> YAGEO; Manufacturer_ID 0805W8F3904T5E -> RC0805FR-073M9L
- R2160: JLCPCB_ID C17668 -> C137516; JLCPCB_STATUS Extended -> (none); Lily_ID 1913-14306 -> NO_ID; Manufacturer Uniroyal Electronics -> YAGEO; Manufacturer_ID 0805W8F4304T5E -> RC0805FR-074M3L
- R2161: JLCPCB_ID C17674 -> C137515; JLCPCB_STATUS Extended -> (none); Lily_ID 1913-14706 -> NO_ID; Manufacturer Uniroyal Electronics -> YAGEO; Manufacturer_ID 0805W8F4704T5E -> RC0805FR-074M7L
- R2162: JLCPCB_ID C26114 -> C137506; JLCPCB_STATUS Extended -> (none); Lily_ID 1913-15106 -> NO_ID; Manufacturer Uniroyal Electronics -> YAGEO; Manufacturer_ID 0805W8F5104T5E -> RC0805FR-075M1L
- R2163: JLCPCB_ID C17728 -> C185285; JLCPCB_STATUS Extended -> (none); Lily_ID 1913-15606 -> NO_ID; Manufacturer Uniroyal Electronics -> YAGEO; Manufacturer_ID 0805W8F5604T5E -> RC0805FR-075M6L
- R2164: JLCPCB_ID C407384 -> C246035; JLCPCB_STATUS Extended -> (none); Lily_ID 1913-16206 -> NO_ID; Manufacturer Uniroyal Electronics -> YAGEO; Manufacturer_ID 0805W8F6204T5E -> RC0805FR-076M2L
- R2165: JLCPCB_ID C17773 -> C137495; JLCPCB_STATUS Extended -> (none); Lily_ID 1913-16806 -> NO_ID; Manufacturer Uniroyal Electronics -> YAGEO; Manufacturer_ID 0805W8F6804T5E -> RC0805FR-076M8L
- R2166: JLCPCB_ID C17808 -> C483221; JLCPCB_STATUS Extended -> (none); Lily_ID 1913-17506 -> NO_ID; Manufacturer Uniroyal Electronics -> YAGEO; Manufacturer_ID 0805W8F7504T5E -> RC0805FR-077M5L
- R2167: JLCPCB_ID C17829 -> C137485; JLCPCB_STATUS Extended -> (none); Lily_ID 1913-18206 -> NO_ID; Manufacturer Uniroyal Electronics -> YAGEO; Manufacturer_ID 0805W8F8204T5E -> RC0805FR-078M2L
- R2168: JLCPCB_ID C17856 -> C274914; JLCPCB_STATUS Extended -> (none); Lily_ID 1913-19106 -> NO_ID; Manufacturer Uniroyal Electronics -> YAGEO; Manufacturer_ID 0805W8F9104T5E -> RC0805FR-079M1L
- R2169: JLCPCB_ID C17477 -> C100045; JLCPCB_STATUS Basic -> (none); Lily_ID 1913-10000 -> NO_ID; Manufacturer Uniroyal Electronics -> YAGEO; Manufacturer_ID 0805W8F0000T5E -> RC0805FR-070RL
